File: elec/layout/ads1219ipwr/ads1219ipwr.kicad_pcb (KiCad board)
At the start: 2 copper layers, 6 parts

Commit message: Build everything with ordered params to fix frozen builds
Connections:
- net DVDD renamed RESETh
- C1 pad 2: gnd-1 -> gnd
- C2 pad 2: gnd-1 -> gnd
- C3 pad 2: gnd -> gnd-1
- U1 pad 1: gnd -> gnd-1
- U1 pad 2: gnd-1 -> gnd
- U3 pad 1: gnd -> gnd-1
- U3 pad 2: gnd -> gnd-1
- U3 pad 4: gnd -> gnd-1
- U3 pad 5: gnd-1 -> gnd
- U3 pad 9: gnd-1 -> gnd
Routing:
- net gnd-1: track 11.1 -> 7.56 mm, vias 1 -> 0
- net gnd: track 7.56 -> 11.1 mm, vias 0 -> 1
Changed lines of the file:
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@@
     (net 3 "AIN0")
     (net 4 "REFN")
-    (net 5 "gnd-1")
+    (net 5 "gnd")
     (net 6 "AIN1")
     (net 7 "AIN3")
-    (net 8 "gnd")
+    (net 8 "gnd-1")
     (net 9 "AIN2")
     (net 10 "SDA")
     (net 11 "hv")
-    (net 12 "DVDD")
+    (net 12 "RESETh")
     (footprint "atopile:TSSOP-16_L5.0-W4.4-P0.65-LS6.4-BL-4f6acc"
         (layer "F.Cu")
@@
             (size 0.34 1.73)
             (layers "F.Cu" "F.Mask" "F.Paste")
-            (net 8 "gnd")
+            (net 8 "gnd-1")
         )
         (pad "2" smd oval
@@
             (size 0.34 1.73)
             (layers "F.Cu" "F.Mask" "F.Paste")
-            (net 8 "gnd")
+            (net 8 "gnd-1")
         )
         (pad "3" smd oval
@@
             (size 0.34 1.73)
             (layers "F.Cu" "F.Mask" "F.Paste")
-            (net 12 "DVDD")
+            (net 12 "RESETh")
         )
         (pad "4" smd oval
@@
             (size 0.34 1.73)
             (layers "F.Cu" "F.Mask" "F.Paste")
-            (net 8 "gnd")
+            (net 8 "gnd-1")
         )
         (pad "5" smd oval
@@
             (size 0.34 1.73)
             (layers "F.Cu" "F.Mask" "F.Paste")
-            (net 5 "gnd-1")
+            (net 5 "gnd")
         )
         (pad "6" smd oval
@@
             (size 0.34 1.73)
             (layers "F.Cu" "F.Mask" "F.Paste")
-            (net 5 "gnd-1")
+            (net 5 "gnd")
         )
         (pad "10" smd oval
@@
             (size 0.34 1.73)
             (layers "F.Cu" "F.Mask" "F.Paste")
-            (net 12 "DVDD")
+            (net 12 "RESETh")
         )
         (pad "14" smd oval
@@
             )
         )
+        (property "PARAM_capacitance" "{\"type\": \"Quantity_Interval_Disjoint\", \"data\": {\"intervals\": {\"type\": \"Numeric_Interval_Disjoint\", \"data\": {\"intervals\": [{\"type\": \"Numeric_Interval\", \"data\": {\"min\": 8.999999985e-06, \"max\": 1.1000000015e-05}}]}}, \"unit\": \"farad\"}}"
+            (at 0 0 0)
+            (layer "User.9")
+            (hide yes)
+            (effects
+                (font
+                    (size 0.125 0.125)
+                    (thickness 0.01875)
+                )
+            )
+        )
+        (property "PARAM_temperature_coefficient" "{\"type\": \"EnumSet\", \"data\": {\"elements\": [{\"name\": \"X5R\"}], \"enum\": {\"name\": \"TemperatureCoefficient\", \"values\": {\"Y5V\": 1, \"Z5U\": 2, \"X7S\": 3, \"X5R\": 4, \"X6R\": 5, \"X7R\": 6, \"X8R\": 7, \"C0G\": 8}}}}"
+            (at 0 0 0)
+            (layer "User.9")
+            (hide yes)
+            (effects
+                (font
+                    (size 0.125 0.125)
+                    (thickness 0.01875)
+                )
+            )
+        )
+        (property "PARAM_max_voltage" "{\"type\": \"Quantity_Set_Discrete\", \"data\": {\"intervals\": {\"type\": \"Numeric_Interval_Disjoint\", \"data\": {\"intervals\": [{\"type\": \"Numeric_Interval\", \"data\": {\"min\": 10.0, \"max\": 10.0}}]}}, \"unit\": \"volt\"}}"
+            (at 0 0 0)
+            (layer "User.9")
+            (hide yes)
+            (effects
+                (font
+                    (size 0.125 0.125)
+                    (thickness 0.01875)
+                )
+            )
+        )
         (attr smd)
         (fp_line
@@
             (size 0.8 0.9)
             (layers "F.Cu" "F.Mask" "F.Paste")
-            (net 5 "gnd-1")
+            (net 5 "gnd")
         )
         (embedded_fonts no)
@@
             )
         )
+        (property "PARAM_capacitance" "{\"type\": \"Quantity_Interval_Disjoint\", \"data\": {\"intervals\": {\"type\": \"Numeric_Interval_Disjoint\", \"data\": {\"intervals\": [{\"type\": \"Numeric_Interval\", \"data\": {\"min\": 9e-08, \"max\": 1.1e-07}}]}}, \"unit\": \"farad\"}}"
+            (at 0 0 0)
+            (layer "User.9")
+            (hide yes)
+            (effects
+                (font
+                    (size 0.125 0.125)
+                    (thickness 0.01875)
+                )
+            )
+        )
+        (property "PARAM_max_voltage" "{\"type\": \"Quantity_Set_Discrete\", \"data\": {\"intervals\": {\"type\": \"Numeric_Interval_Disjoint\", \"data\": {\"intervals\": [{\"type\": \"Numeric_Interval\", \"data\": {\"min\": 16.0, \"max\": 16.0}}]}}, \"unit\": \"volt\"}}"
+            (at 0 0 0)
+            (layer "User.9")
+            (hide yes)
+            (effects
+                (font
+                    (size 0.125 0.125)
+                    (thickness 0.01875)
+                )
+            )
+        )
+        (property "PARAM_temperature_coefficient" "{\"type\": \"EnumSet\", \"data\": {\"elements\": [{\"name\": \"X7R\"}], \"enum\": {\"name\": \"TemperatureCoefficient\", \"values\": {\"Y5V\": 1, \"Z5U\": 2, \"X7S\": 3, \"X5R\": 4, \"X6R\": 5, \"X7R\": 6, \"X8R\": 7, \"C0G\": 8}}}}"
+            (at 0 0 0)
+            (layer "User.9")
+            (hide yes)
+            (effects
+                (font
+                    (size 0.125 0.125)
+                    (thickness 0.01875)
+                )
+            )
+        )
         (attr smd)
         (fp_line
@@
             (size 0.79 0.54)
             (layers "F.Cu" "F.Mask" "F.Paste")
-            (net 12 "DVDD")
+            (net 12 "RESETh")
         )
         (pad "2" smd rect
@@
             (size 0.79 0.54)
             (layers "F.Cu" "F.Mask" "F.Paste")
-            (net 8 "gnd")
+            (net 8 "gnd-1")
         )
         (embedded_fonts no)
@@
             (size 0.25 0.25)
             (layers "F.Cu")
-            (net 12 "DVDD")
+            (net 12 "RESETh")
         )
         (embedded_fonts no)
@@
             (size 0.25 0.25)
             (layers "F.Cu")
-            (net 8 "gnd")
+            (net 8 "gnd-1")
         )
         (pad "2" smd circle
@@
             (size 0.25 0.25)
             (layers "F.Cu")
-            (net 5 "gnd-1")
+            (net 5 "gnd")
         )
         (embedded_fonts no)
@@
             )
         )
+        (property "PARAM_capacitance" "{\"type\": \"Quantity_Interval_Disjoint\", \"data\": {\"intervals\": {\"type\": \"Numeric_Interval_Disjoint\", \"data\": {\"intervals\": [{\"type\": \"Numeric_Interval\", \"data\": {\"min\": 9e-08, \"max\": 1.1e-07}}]}}, \"unit\": \"farad\"}}"
+            (at 0 0 0)
+            (layer "User.9")
+            (hide yes)
+            (effects
+                (font
+                    (size 0.125 0.125)
+                    (thickness 0.01875)
+                )
+            )
+        )
+        (property "PARAM_temperature_coefficient" "{\"type\": \"EnumSet\", \"data\": {\"elements\": [{\"name\": \"X7R\"}], \"enum\": {\"name\": \"TemperatureCoefficient\", \"values\": {\"Y5V\": 1, \"Z5U\": 2, \"X7S\": 3, \"X5R\": 4, \"X6R\": 5, \"X7R\": 6, \"X8R\": 7, \"C0G\": 8}}}}"
+            (at 0 0 0)
+            (layer "User.9")
+            (hide yes)
+            (effects
+                (font
+                    (size 0.125 0.125)
+                    (thickness 0.01875)
+                )
+            )
+        )
+        (property "PARAM_max_voltage" "{\"type\": \"Quantity_Set_Discrete\", \"data\": {\"intervals\": {\"type\": \"Numeric_Interval_Disjoint\", \"data\": {\"intervals\": [{\"type\": \"Numeric_Interval\", \"data\": {\"min\": 16.0, \"max\": 16.0}}]}}, \"unit\": \"volt\"}}"
+            (at 0 0 0)
+            (layer "User.9")
+            (hide yes)
+            (effects
+                (font
+                    (size 0.125 0.125)
+                    (thickness 0.01875)
+                )
+            )
+        )
         (attr smd)
         (fp_line
@@
             (size 0.79 0.54)
             (layers "F.Cu" "F.Mask" "F.Paste")
-            (net 5 "gnd-1")
+            (net 5 "gnd")
         )
         (embedded_fonts no)

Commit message: checkin
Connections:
- net RESETh renamed DVDD
- C1 pad 2: gnd -> gnd-1
- C2 pad 2: gnd -> gnd-1
- C3 pad 2: gnd-1 -> gnd
- U1 pad 1: gnd-1 -> gnd
- U1 pad 2: gnd -> gnd-1
- U3 pad 1: gnd-1 -> gnd
- U3 pad 2: gnd-1 -> gnd
- U3 pad 4: gnd-1 -> gnd
- U3 pad 5: gnd -> gnd-1
- U3 pad 9: gnd -> gnd-1
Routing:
- net gnd-1: track 7.56 -> 11.1 mm, vias 0 -> 1
- net gnd: track 11.1 -> 7.56 mm, vias 1 -> 0
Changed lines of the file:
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@@
     (net 3 "AIN0")
     (net 4 "REFN")
-    (net 5 "gnd")
+    (net 5 "gnd-1")
     (net 6 "AIN1")
     (net 7 "AIN3")
-    (net 8 "gnd-1")
+    (net 8 "gnd")
     (net 9 "AIN2")
     (net 10 "SDA")
     (net 11 "hv")
-    (net 12 "RESETh")
+    (net 12 "DVDD")
     (footprint "atopile:TSSOP-16_L5.0-W4.4-P0.65-LS6.4-BL-4f6acc"
         (layer "F.Cu")
@@
             (size 0.34 1.73)
             (layers "F.Cu" "F.Mask" "F.Paste")
-            (net 8 "gnd-1")
+            (net 8 "gnd")
         )
         (pad "2" smd oval
@@
             (size 0.34 1.73)
             (layers "F.Cu" "F.Mask" "F.Paste")
-            (net 8 "gnd-1")
+            (net 8 "gnd")
         )
         (pad "3" smd oval
@@
             (size 0.34 1.73)
             (layers "F.Cu" "F.Mask" "F.Paste")
-            (net 12 "RESETh")
+            (net 12 "DVDD")
         )
         (pad "4" smd oval
@@
             (size 0.34 1.73)
             (layers "F.Cu" "F.Mask" "F.Paste")
-            (net 8 "gnd-1")
+            (net 8 "gnd")
         )
         (pad "5" smd oval
@@
             (size 0.34 1.73)
             (layers "F.Cu" "F.Mask" "F.Paste")
-            (net 5 "gnd")
+            (net 5 "gnd-1")
         )
         (pad "6" smd oval
@@
             (size 0.34 1.73)
             (layers "F.Cu" "F.Mask" "F.Paste")
-            (net 5 "gnd")
+            (net 5 "gnd-1")
         )
         (pad "10" smd oval
@@
             (size 0.34 1.73)
             (layers "F.Cu" "F.Mask" "F.Paste")
-            (net 12 "RESETh")
+            (net 12 "DVDD")
         )
         (pad "14" smd oval
@@
             (size 0.8 0.9)
             (layers "F.Cu" "F.Mask" "F.Paste")
-            (net 5 "gnd")
+            (net 5 "gnd-1")
         )
         (embedded_fonts no)
@@
             (size 0.79 0.54)
             (layers "F.Cu" "F.Mask" "F.Paste")
-            (net 12 "RESETh")
+            (net 12 "DVDD")
         )
         (pad "2" smd rect
@@
             (size 0.79 0.54)
             (layers "F.Cu" "F.Mask" "F.Paste")
-            (net 8 "gnd-1")
+            (net 8 "gnd")
         )
         (embedded_fonts no)
@@
             (size 0.25 0.25)
             (layers "F.Cu")
-            (net 12 "RESETh")
+            (net 12 "DVDD")
         )
         (embedded_fonts no)
@@
             (size 0.25 0.25)
             (layers "F.Cu")
-            (net 8 "gnd-1")
+            (net 8 "gnd")
         )
         (pad "2" smd circle
@@
             (size 0.25 0.25)
             (layers "F.Cu")
-            (net 5 "gnd")
+            (net 5 "gnd-1")
         )
         (embedded_fonts no)
@@
             (size 0.79 0.54)
             (layers "F.Cu" "F.Mask" "F.Paste")
-            (net 5 "gnd")
+            (net 5 "gnd-1")
         )
         (embedded_fonts no)

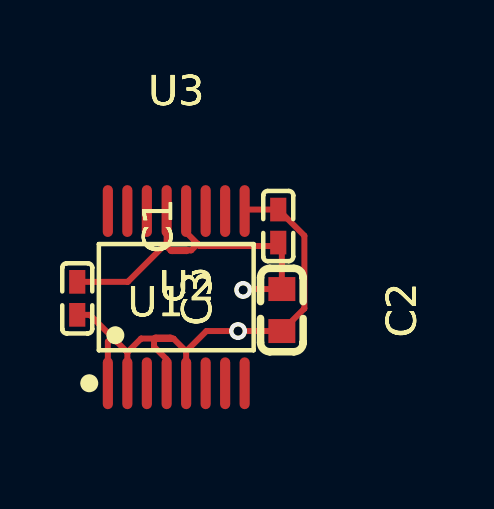
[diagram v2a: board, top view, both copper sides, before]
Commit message: add addressor to ads1219 adc
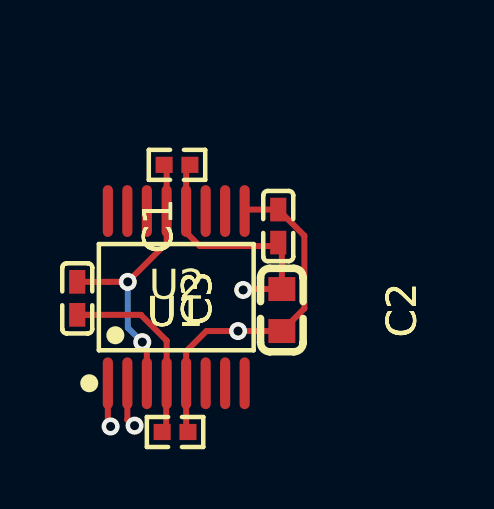
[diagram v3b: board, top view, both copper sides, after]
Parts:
- U1, U2: value (none) -> 0Ω 62.5mW; footprint lib:NetTie-2_SMD_Pad0.25mm -> atopile:R0402-56259e
- moved U1 3.19 mm to (154.1, 110.6)
- moved U2 2.87 mm to (154.2, 101.7)
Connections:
- net DVDD renamed hv-1
- C1 pad 2: gnd-1 -> gnd
- C2 pad 2: gnd-1 -> gnd
- C3 pad 2: gnd -> gnd-1
- U1 pad 1: gnd -> gnd-1
- U1 pad 2: gnd-1 -> gnd
- U3 pad 1: gnd -> A0
- U3 pad 2: gnd -> A1
- U3 pad 4: gnd -> gnd-1
- U3 pad 5: gnd-1 -> gnd
- U3 pad 9: gnd-1 -> gnd
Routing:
- net hv-1: track 5.03 -> 9.80 mm, vias 0 -> 2
- net gnd-1: track 11.1 -> 6.58 mm, vias 1 -> 0
- net gnd: track 7.56 -> 12.0 mm, vias 0 -> 1
- net A1: track 0.00 -> 1.54 mm, vias 0 -> 1
- net A0: track 0.00 -> 1.48 mm, vias 0 -> 1
- net hv: track 7.47 -> 8.51 mm
